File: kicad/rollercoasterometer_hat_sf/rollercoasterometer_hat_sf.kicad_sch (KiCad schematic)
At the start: 13 parts, among them J101 Raspberry_Pi_40, J102 Conn_01x03, J103 LSD9DS1, J104 ICM20948, J105 BME680, U101 RaspberryPi 4B 2GB

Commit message: Commit as-ordered shipometer 23.03
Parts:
- added D101, D102, D103, D104: White, LED_SMD:LED_0603_1608Metric, symbol Device:LED_Small
- added U102: 74LS138, Package_SO:TSSOP-16_4.4x5mm_P0.65mm, symbol 74xx:74LS138
- G103, G107: value DesignedWithKicad -> Designed with
- J101, J102: Number in cart (none) -> 1; Number on hand (none) -> 0
- J103: value LSD9DS1 -> LSM9DS1; Number on hand (none) -> 1
- J104, J105, U101: Number on hand (none) -> 1
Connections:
- net +3V3: now also D101.2 (A), D102.2 (A), D103.2 (A), D104.2 (A), U102.16 (VCC), U102.6 (E3)
- net DRDY_6D: now also J101.31 (GPIO6)
- net DRDY_MAG: now also J101.22 (GPIO25_(GEN6))
- net GND: now also U102.8 (GND)
- net GPS_RX: now also J101.29 (GPIO5); no longer J101.8 ((TXD0)_GPIO14)
- net GPS_TX: now also J101.7 ((GCLK)_GPIO4); no longer J101.10 ((RXD0)_GPIO15)
- net LPC_RX: now also J101.8 ((TXD0)_GPIO14); no longer J101.32 ((PWM0)_GPIO12)
- net LPC_TX: now also J101.10 ((RXD0)_GPIO15); no longer J101.33 ((PWM1)_GPIO13)
- net LPC_~{BOOTSTRAP}: now also J101.18 (GPIO24_(GEN5))
- net LPC_~{RESET}: now also J101.16 (GPIO23_(GEN4)); no longer J101.11 (GPIO17_(GEN0))
- net ~{CE0}: now also U102.4 (E1), U102.5 (E2)
- net ~{CS}_6D: now also D101.1 (K), U102.15 (O0)
- net ~{CS}_LPC_3V3: now also D104.1 (K), U102.12 (O3)
- net ~{CS}_MAG: now also D102.1 (K), U102.14 (O1)
- net ~{CS}_PRES: now also D103.1 (K), U102.13 (O2)
- net CS_A1: now reaches J101.13 (GPIO27_(GEN2))
- net CS_A1: now also U102.2 (A1)
- net CS_A0: now reaches J101.15 (GPIO22_(GEN3))
- net CS_A0: now also U102.1 (A0)
- net CS0: no longer names the net of J101.37 (GPIO26)
- net CS1: no longer names the net of J101.35 ((MISO)_GPIO19)
- new net CS_A2: J101.11 (GPIO17_(GEN0)), U102.3 (A2)
- no-connect marks 31 -> 30
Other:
- removed sheet Bus Level Converter
- removed sheet Shoe
- removed sheet USB+ Cable
- added sheet USB C Cable (../kwan_kicad_lib/blocks/USB_C.kicad_sch)
- note added: "Chip Select"
- note added: "Designed to drive multiple SPI devices with a single SPI port. Use arbitrary GPIO pins in output to create an address bus. Decoder is one-low. Output will be all-high until ~{CE} is asserted, at which time the one selected output will be low and can be used as ~{CS} for an SPI slave."
- note added: "Leave I2C free in case we decide to use it later"
- note added: "Multiple GPIOs can be hooked to PPS, and signals do not have to run at one pulse per second. PPS needs to be enabled in /boot/config.txt. The order of the devices is the reverse of the order in config.txt, IE if two pins are specified, the first pin is /dev/pps1 and the second is /dev/pps0. Higher numbered PPS devices. GPS PPS must be hooked to whatever comes up as /dev/pps0."
- note removed: "CS0 CS1 CS2 CS3"

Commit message: Updated to KiCad 7.0
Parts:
- D101, D102, D103, D104: Number in cart 10 -> (none); Number on hand 0 -> 10
- J101, J102: Number in cart 1 -> (none); Number on hand 0 -> 1

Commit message: Starting to make gps_breakout
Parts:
- added J106: ZED-F9R, symbol Sparkfun_Breakout:ZED-F9R
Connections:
- net +5V: now also J106.2 (5V)
- net GND: now also J106.1 (GND), J106.12 (GND)
- net GPS_RX: now also J106.5 (RX/MOSI)
- net GPS_TX: now also J106.6 (TX/MISO)
- net PPS: now also J106.20 (PPS)
- new net 3V3: J106.13 (3V3), J106.3 (3V3)
- no-connect marks 30 -> 42
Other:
- removed sheet GPS
- removed sheet USB C Cable

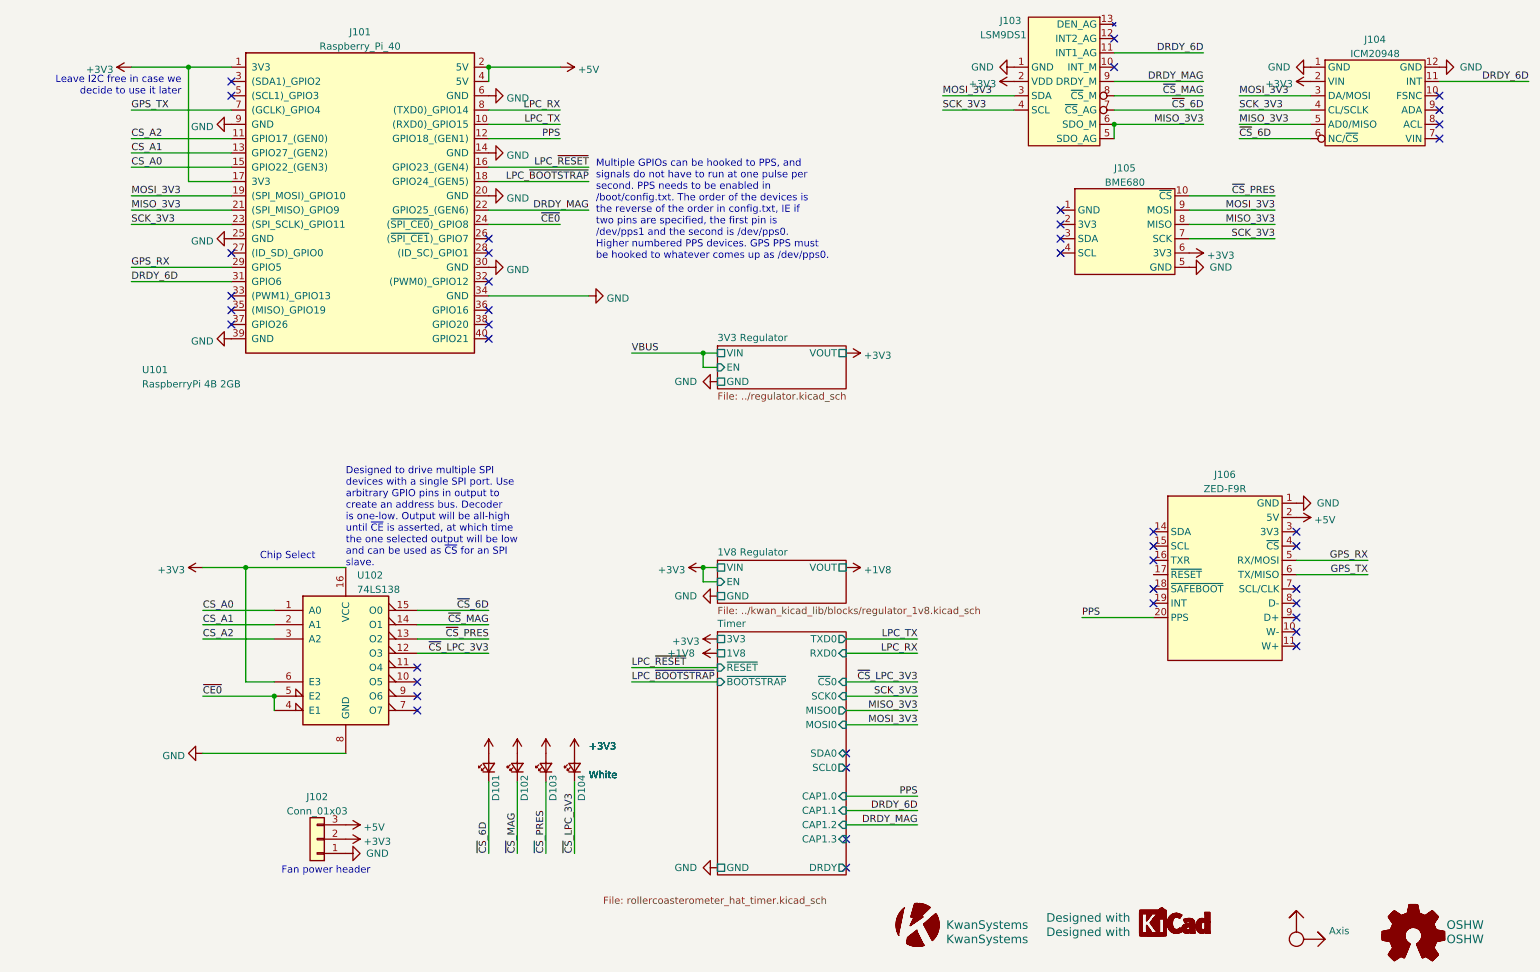
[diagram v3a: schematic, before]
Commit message: Added BME280 and ICM20948 stamps
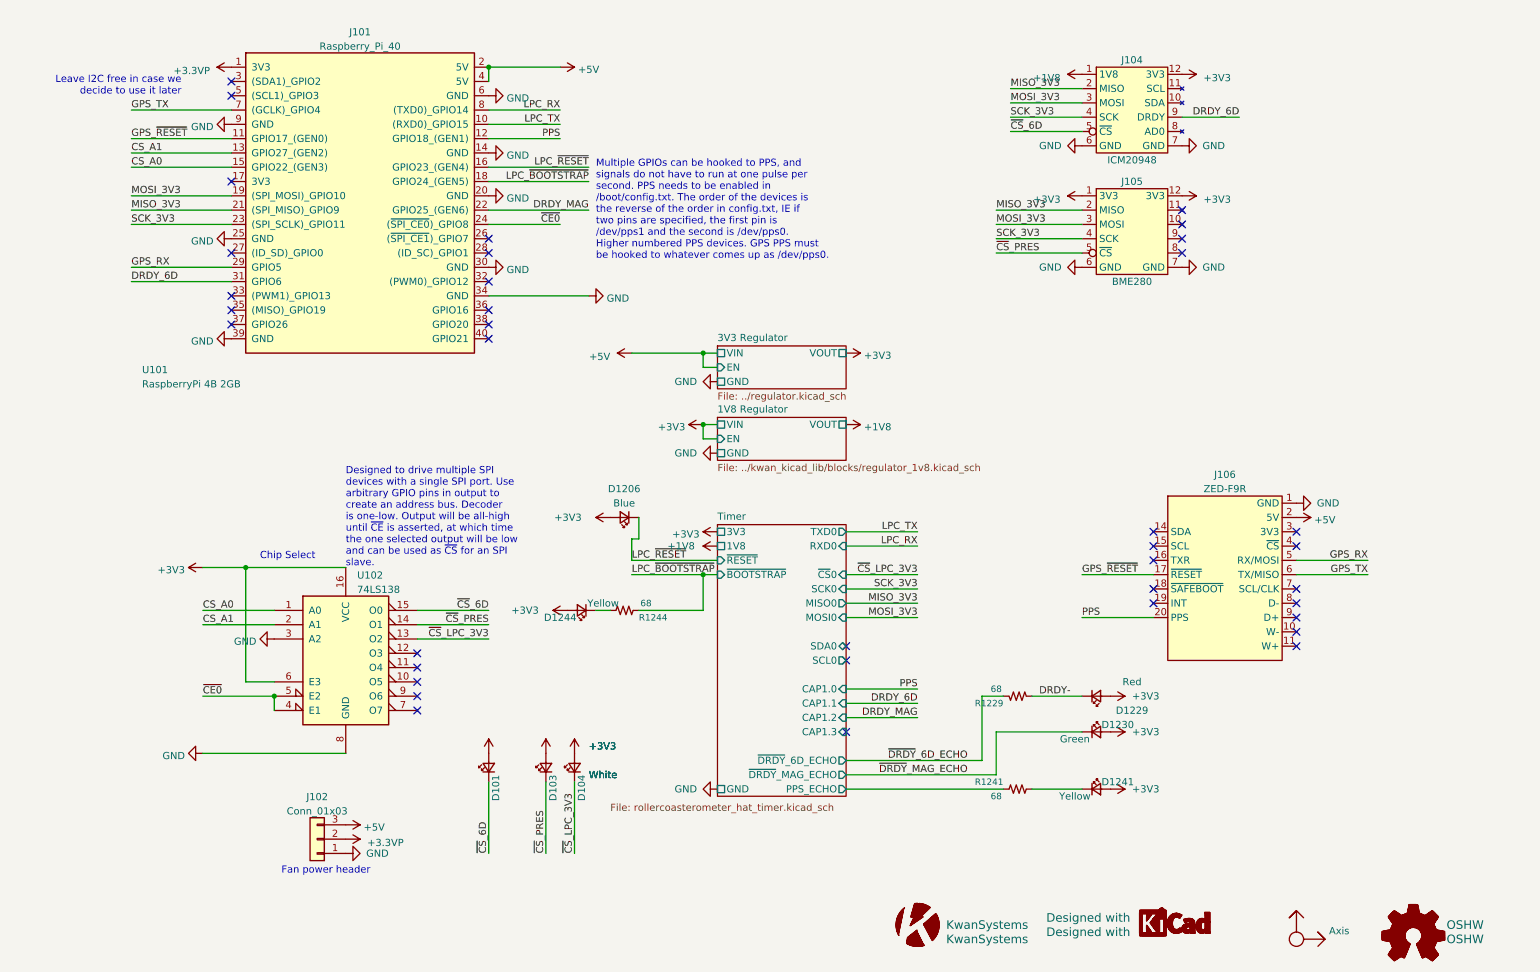
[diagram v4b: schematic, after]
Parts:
- removed D102: White, LED_SMD:LED_0603_1608Metric, symbol Device:LED_Small
- removed J103: LSM9DS1, SparkfunBreakout:LSM9DS1, symbol Sparkfun_Breakout:LSM9DS1
- removed J104: ICM20948, SparkfunBreakout:ICM20948, symbol Sparkfun_Breakout:ICM20948
- removed J105: BME680, SparkfunBreakout:BME680, symbol Sparkfun_Breakout:BME680
- added D1206: Blue, LED_SMD:LED_0603_1608Metric, symbol Device:LED_Small
- added D1229: Red, LED_SMD:LED_0603_1608Metric, symbol Device:LED_Small
- added D1230: Green, LED_SMD:LED_0603_1608Metric, symbol Device:LED_Small
- added D1241, D1244: Yellow, LED_SMD:LED_0603_1608Metric, symbol Device:LED_Small
- added J104: ICM20948, KwanSystems:StampPad, symbol KwanSystems:STAMP
- added J105: BME280, KwanSystems:StampPad, symbol KwanSystems:STAMP
- added R1229, R1241, R1244: 68, Resistor_SMD:R_0603_1608Metric, symbol KwanSystems:RESISTOR
- J106: footprint (none) -> SparkfunBreakout:ZED-F9R
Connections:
- net ~{CS}_MAG is gone; now on net ~{CS}_PRES: U102.14 (O1)
- net +1V8: now also J104.1 (1V8)
- net +3V3: now also D1206.2 (A), D1229.2 (A), D1230.2 (A), D1241.2 (A), D1244.2 (A), J104.12 (3V3), J105.1 (3V3), J105.12 (3V3); no longer J101.1 (3V3), J101.17 (3V3), J102.2 (Pin_2)
- net DRDY_6D: now also J104.9 (DRDY)
- net GND: now also U102.3 (A2), J104.6 (GND), J104.7 (GND), J105.6 (GND), J105.7 (GND)
- net LPC_~{BOOTSTRAP}: now also R1244.1
- net LPC_~{RESET}: now also D1206.1 (K)
- net MISO_3V3: now also J104.2 (MISO), J105.2 (MISO)
- net MOSI_3V3: now also J104.3 (MOSI), J105.3 (MOSI)
- net SCK_3V3: now also J104.4 (SCK), J105.4 (SCK)
- net ~{CS}_6D: now also J104.5 (~{CS})
- net ~{CS}_LPC_3V3: now also U102.13 (O2); no longer U102.12 (O3)
- net ~{CS}_PRES: now also J105.5 (~{CS}); no longer U102.13 (O2)
- net GPS_~{RESET}: now reaches J106.17 (~{RESET})
- net GPS_~{RESET}: now also J101.11 (GPIO17_(GEN0))
- removed net CS_A2: J101.11 (GPIO17_(GEN0)), U102.3 (A2)
- new net: D1244.1 (K), R1244.2
- new net: D1241.1 (K), R1241.2
- new net +3.3VP: J101.1 (3V3), J102.2 (Pin_2)
- new net DRDY-: D1229.1 (K), R1229.2
- new net Timer/PPS_ECHO: R1241.1
- new net ~{DRDY}_6D_ECHO: R1229.1
- new net ~{DRDY}_MAG_ECHO: D1230.1 (K)
- no-connect marks 42 -> 37
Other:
- sheet Timer ports: added PPS_ECHO, ~{DRDY}_6D_ECHO, ~{DRDY}_MAG_ECHO; removed DRDY

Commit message: As ordered on 03 Apr 2023. Some but not all numbers-on-hand have been updated.
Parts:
- removed R1229, R1241, R1244: 68, Resistor_SMD:R_0603_1608Metric, symbol KwanSystems:RESISTOR
- added R101, R102: 68, KwanSystems:R_Array_Convex_4x0402, symbol KwanSystems:RP4
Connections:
- net DRDY-: now also R102.5
- net LPC_~{BOOTSTRAP}: now also R102.2 (4)
- net ~{CS}_6D: now also R101.1 (4); no longer D101.1 (K)
- net ~{CS}_PRES: now also R101.2 (4); no longer D103.1 (K)
- net ~{DRDY}_6D_ECHO: now also R102.4
- net ~{DRDY}_MAG_ECHO: now also R102.3 (4); no longer D1230.1 (K)
- net BOOTSTRAP-: now reaches D1244.1 (K)
- net BOOTSTRAP-: now also R102.7 (5)
- net PPS-: now reaches D1241.1 (K)
- net PPS-: now also R101.5
- net ~{CS}_LPC_3V3 renamed ~{CS}_LPC
- net ~{CS}_LPC: now also R101.3 (4); no longer D104.1 (K)
- new net DRDY_MAG-: D1230.1 (K), R102.6 (5)
- new net ~{CS}_6D+: D101.1 (K), R101.8 (5)
- new net ~{CS}_LPC+: D104.1 (K), R101.6 (5)
- new net ~{CS}_PRES+: D103.1 (K), R101.7 (5)
- new net ~{PPS}_ECHO: R101.4
- no-connect marks 37 -> 39
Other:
- note added: "Red, yellow, green, and white diodes get 68R. Blue doesn't need a resistor."
